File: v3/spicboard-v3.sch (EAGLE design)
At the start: 39 parts, among them IC1 74HC595N, Q1 BC557, Q2 BC557

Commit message: OLED1 ausgetauscht
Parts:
- OLED1: device pinhead:PINHD-1X4 -> SparkFun-Connectors:CONN_04
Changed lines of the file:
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@@
 <part name="GND7" library="supply1" deviceset="GND" device=""/>
 <part name="EXT" library="pinhead" deviceset="PINHD-1X4" device=""/>
-<part name="OLED1" library="pinhead" deviceset="PINHD-1X4" device=""/>
 <part name="OLED2" library="pinhead" deviceset="PINHD-1X4" device=""/>
 <part name="COM" library="pinhead" deviceset="PINHD-1X3" device=""/>
@@
 <part name="BTN0" library="switch-omron" deviceset="10-XX" device=""/>
 <part name="BTN1" library="switch-omron" deviceset="10-XX" device=""/>
+<part name="OLED1" library="SparkFun-Connectors" deviceset="CONN_04" device=""/>
 </parts>
 <sheets>
@@
 <instance part="GND7" gate="1" x="137.16" y="-10.16"/>
 <instance part="EXT" gate="A" x="48.26" y="-20.32"/>
-<instance part="OLED1" gate="A" x="48.26" y="-2.54"/>
 <instance part="OLED2" gate="A" x="81.28" y="-2.54"/>
 <instance part="COM" gate="A" x="81.28" y="-17.78"/>
@@
 <instance part="BTN0" gate="1" x="129.54" y="0"/>
 <instance part="BTN1" gate="1" x="172.72" y="0"/>
+<instance part="OLED1" gate="G$1" x="43.18" y="0" rot="R180"/>
 </instances>
 <busses>
@@
 </segment>
 <segment>
-<pinref part="OLED1" gate="A" pin="2"/>
-<wire x1="27.94" y1="0" x2="45.72" y2="0" width="0.1524" layer="91"/>
+<wire x1="27.94" y1="0" x2="38.1" y2="0" width="0.1524" layer="91"/>
 <label x="27.94" y="0" size="1.778" layer="95"/>
+<pinref part="OLED1" gate="G$1" pin="2"/>
 </segment>
 <segment>
@@
 </segment>
 <segment>
-<pinref part="OLED1" gate="A" pin="1"/>
-<wire x1="45.72" y1="2.54" x2="27.94" y2="2.54" width="0.1524" layer="91"/>
 <label x="27.94" y="2.54" size="1.778" layer="95"/>
+<pinref part="OLED1" gate="G$1" pin="1"/>
+<wire x1="38.1" y1="2.54" x2="27.94" y2="2.54" width="0.1524" layer="91"/>
 </segment>
 <segment>
@@
 </segment>
 <segment>
-<pinref part="OLED1" gate="A" pin="4"/>
-<wire x1="27.94" y1="-5.08" x2="45.72" y2="-5.08" width="0.1524" layer="91"/>
+<wire x1="27.94" y1="-5.08" x2="38.1" y2="-5.08" width="0.1524" layer="91"/>
 <label x="27.94" y="-5.08" size="1.778" layer="95"/>
+<pinref part="OLED1" gate="G$1" pin="4"/>
 </segment>
 <segment>
@@
 </segment>
 <segment>
-<pinref part="OLED1" gate="A" pin="3"/>
-<wire x1="45.72" y1="-2.54" x2="27.94" y2="-2.54" width="0.1524" layer="91"/>
 <label x="27.94" y="-2.54" size="1.778" layer="95"/>
-</segment>
-<segment>
+<pinref part="OLED1" gate="G$1" pin="3"/>
+<wire x1="38.1" y1="-2.54" x2="27.94" y2="-2.54" width="0.1524" layer="91"/>
+</segment>
+<segment>

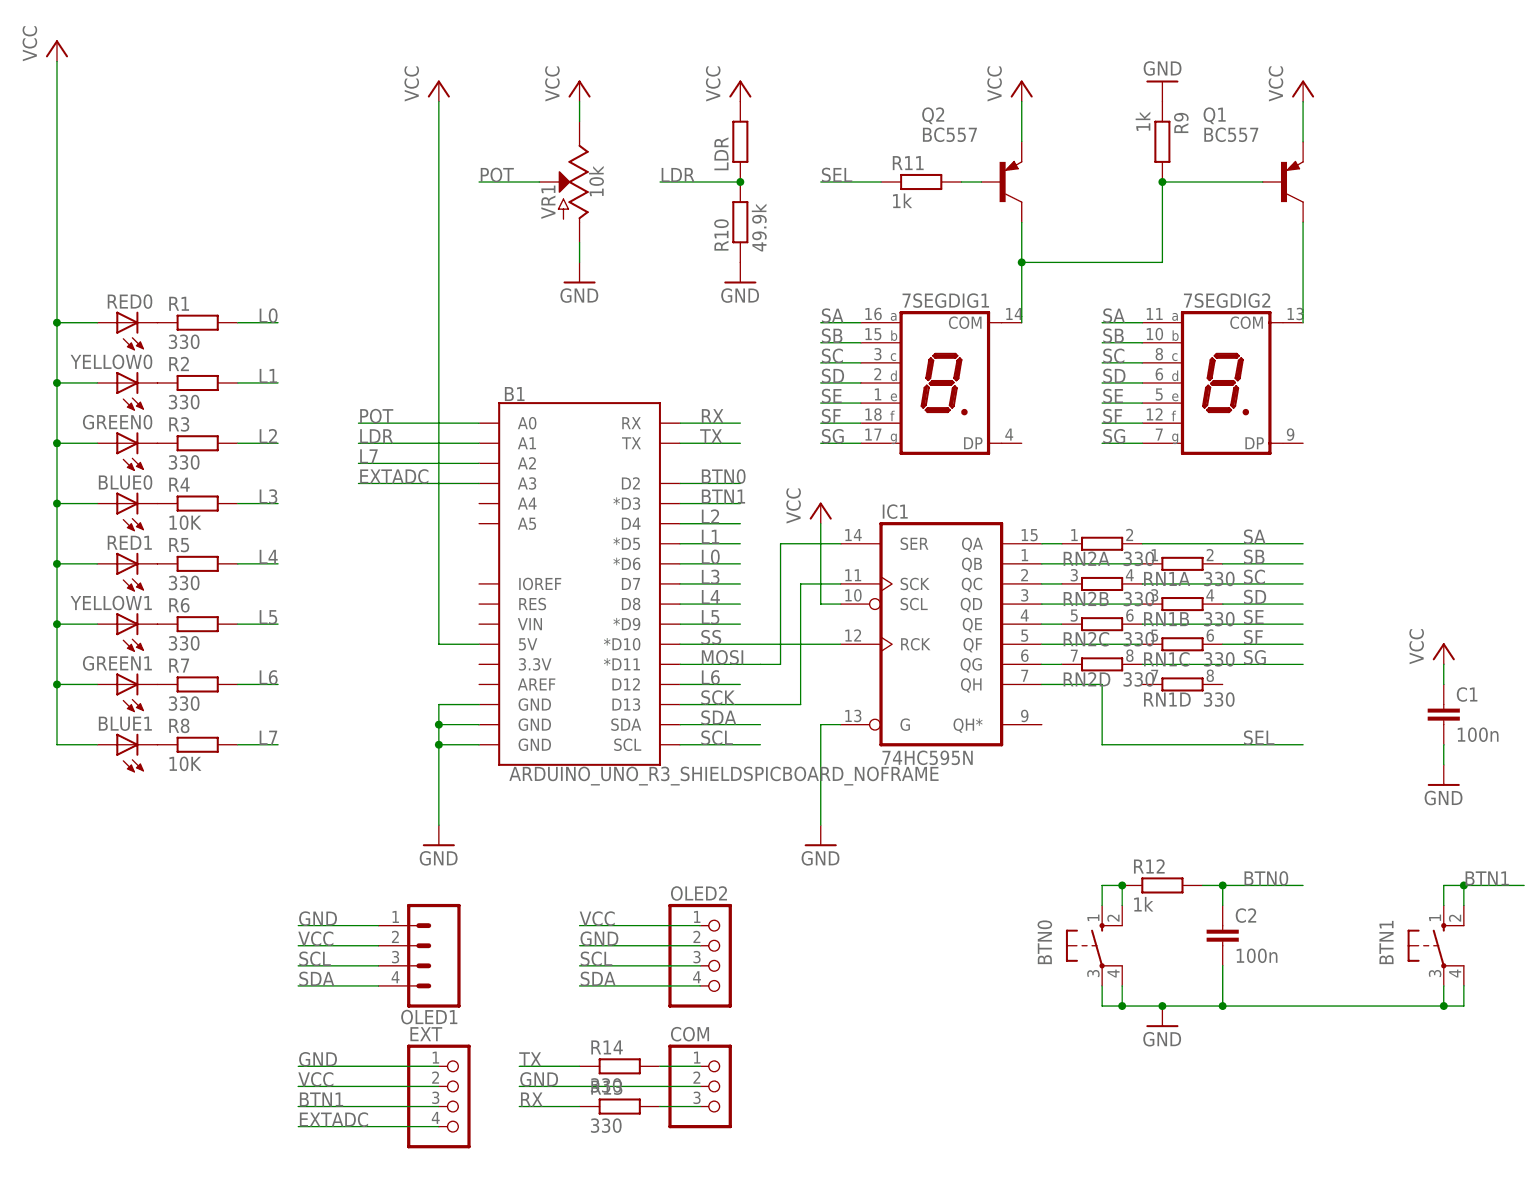
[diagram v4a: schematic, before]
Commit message: OLED/EXT/COM ausgetauscht
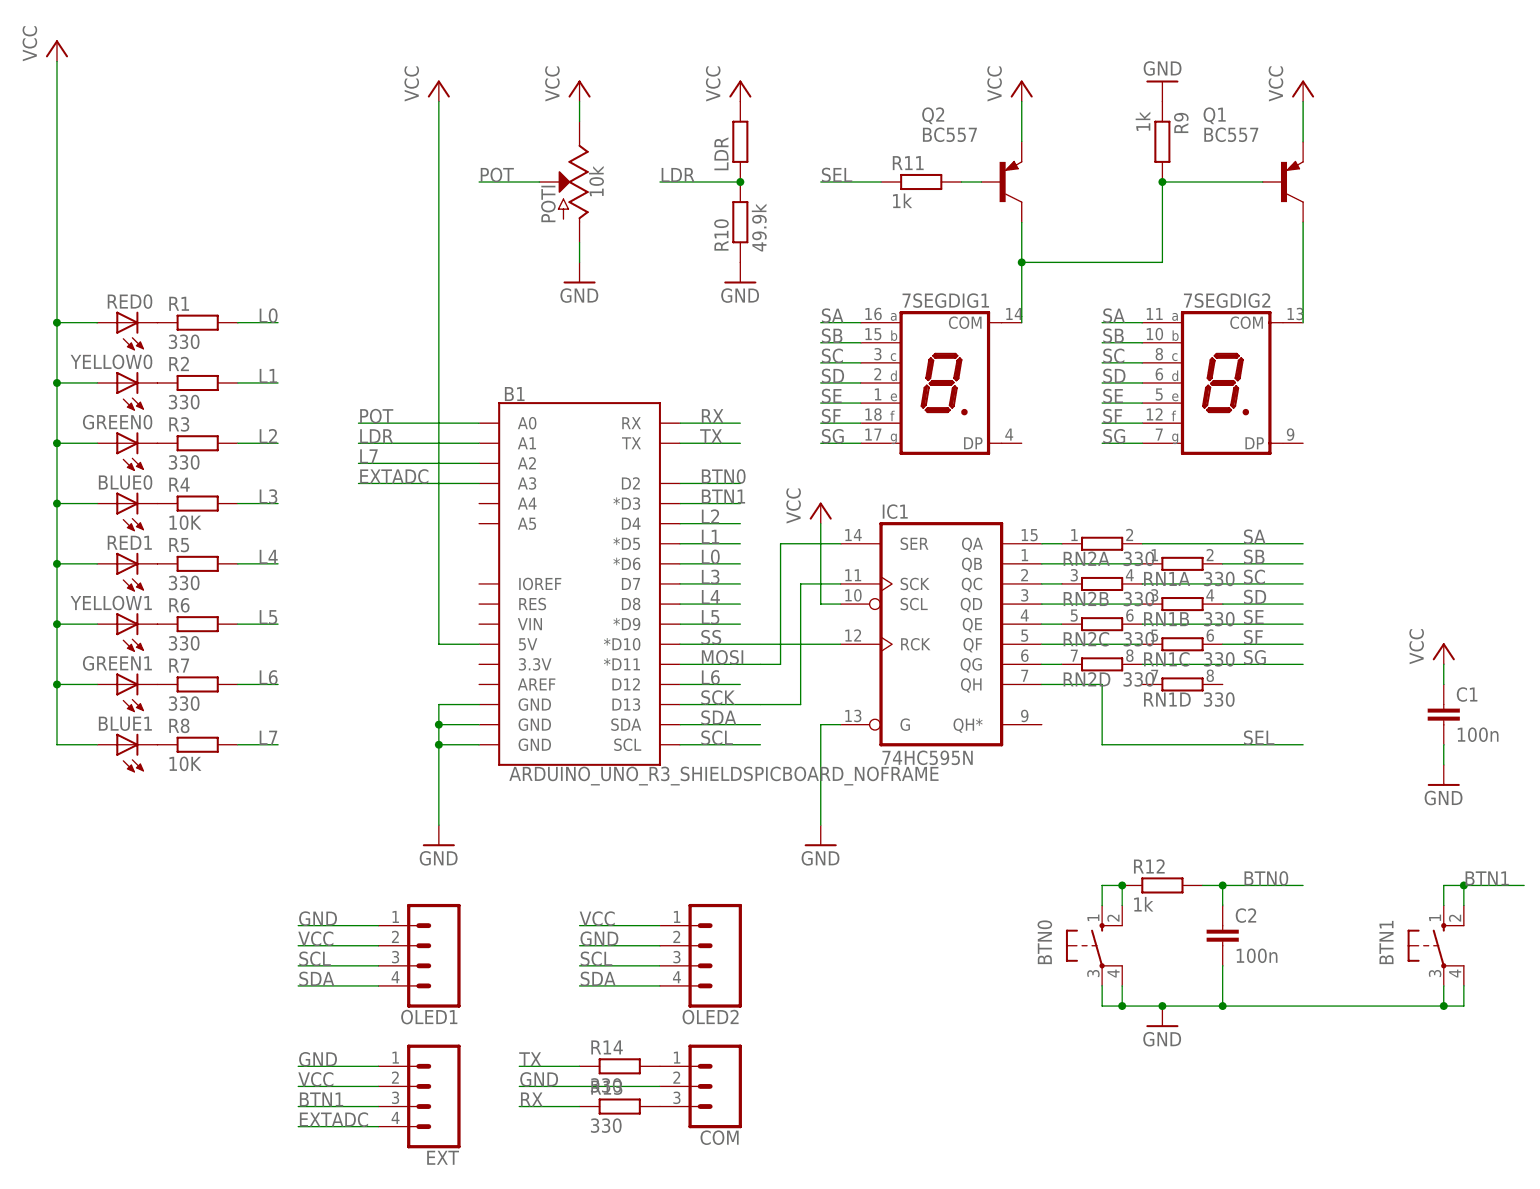
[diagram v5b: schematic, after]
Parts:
- COM: device pinhead:PINHD-1X3 -> SparkFun-Connectors:CONN_03
- EXT, OLED2: device pinhead:PINHD-1X4 -> SparkFun-Connectors:CONN_04
- renumbered VR1 to POTI
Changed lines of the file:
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@@
 <part name="IC1" library="74xx-eu" deviceset="74*595" device="N" technology="HC"/>
 <part name="LDR" library="spicboard-v3" deviceset="LDR" device="LDR" value=""/>
-<part name="VR1" library="spicboard-v3" deviceset="POTENTIOMETER" device="-PTH-9MM-1/20W-20%" value="10k"/>
+<part name="POTI" library="spicboard-v3" deviceset="POTENTIOMETER" device="-PTH-9MM-1/20W-20%" value="10k"/>
 <part name="RN1" library="resistor-sil" deviceset="E4R" device="" value="330"/>
 <part name="RN2" library="resistor-sil" deviceset="E4R" device="" value="330"/>
@@
 <part name="C2" library="capacitor-wima" deviceset="C" device="2.5/2" value="100n"/>
 <part name="GND7" library="supply1" deviceset="GND" device=""/>
-<part name="EXT" library="pinhead" deviceset="PINHD-1X4" device=""/>
-<part name="OLED2" library="pinhead" deviceset="PINHD-1X4" device=""/>
-<part name="COM" library="pinhead" deviceset="PINHD-1X3" device=""/>
 <part name="R13" library="resistor" deviceset="R-EU_" device="0207/10" value="330"/>
 <part name="R14" library="resistor" deviceset="R-EU_" device="0207/10" value="330"/>
@@
 <part name="BTN1" library="switch-omron" deviceset="10-XX" device=""/>
 <part name="OLED1" library="SparkFun-Connectors" deviceset="CONN_04" device=""/>
+<part name="OLED2" library="SparkFun-Connectors" deviceset="CONN_04" device=""/>
+<part name="EXT" library="SparkFun-Connectors" deviceset="CONN_04" device=""/>
+<part name="COM" library="SparkFun-Connectors" deviceset="CONN_03" device=""/>
 </parts>
 <sheets>
@@
 <instance part="IC1" gate="A" x="109.22" y="40.64"/>
 <instance part="LDR" gate="G$1" x="83.82" y="101.6" rot="R90"/>
-<instance part="VR1" gate="G$1" x="63.5" y="96.52" rot="MR0"/>
+<instance part="POTI" gate="G$1" x="63.5" y="96.52" rot="MR0"/>
 <instance part="RN1" gate="A" x="139.7" y="48.26"/>
 <instance part="RN1" gate="B" x="139.7" y="43.18"/>
@@
 <instance part="C2" gate="G$1" x="144.78" y="2.54"/>
 <instance part="GND7" gate="1" x="137.16" y="-10.16"/>
-<instance part="EXT" gate="A" x="48.26" y="-20.32"/>
-<instance part="OLED2" gate="A" x="81.28" y="-2.54"/>
-<instance part="COM" gate="A" x="81.28" y="-17.78"/>
 <instance part="R13" gate="G$1" x="68.58" y="-20.32"/>
 <instance part="R14" gate="G$1" x="68.58" y="-15.24"/>
@@
 <instance part="BTN1" gate="1" x="172.72" y="0"/>
 <instance part="OLED1" gate="G$1" x="43.18" y="0" rot="R180"/>
+<instance part="OLED2" gate="G$1" x="78.74" y="0" rot="R180"/>
+<instance part="EXT" gate="G$1" x="43.18" y="-17.78" rot="R180"/>
+<instance part="COM" gate="J$1" x="81.28" y="-17.78" rot="R180"/>
 </instances>
 <busses>
@@
 </segment>
 <segment>
-<pinref part="VR1" gate="G$1" pin="E"/>
+<pinref part="POTI" gate="G$1" pin="E"/>
 <pinref part="P+4" gate="VCC" pin="VCC"/>
 <wire x1="63.5" y1="104.14" x2="63.5" y2="106.68" width="0.1524" layer="91"/>
@@
 </segment>
 <segment>
-<pinref part="OLED2" gate="A" pin="1"/>
-<wire x1="78.74" y1="2.54" x2="63.5" y2="2.54" width="0.1524" layer="91"/>
+<wire x1="73.66" y1="2.54" x2="63.5" y2="2.54" width="0.1524" layer="91"/>
 <label x="63.5" y="2.54" size="1.778" layer="95"/>
-</segment>
-<segment>
-<pinref part="EXT" gate="A" pin="2"/>
-<wire x1="45.72" y1="-17.78" x2="27.94" y2="-17.78" width="0.1524" layer="91"/>
+<pinref part="OLED2" gate="G$1" pin="1"/>
+</segment>
+<segment>
+<wire x1="38.1" y1="-17.78" x2="27.94" y2="-17.78" width="0.1524" layer="91"/>
 <label x="27.94" y="-17.78" size="1.778" layer="95"/>
+<pinref part="EXT" gate="G$1" pin="2"/>
 </segment>
 <segment>
@@
 </segment>
 <segment>
-<pinref part="VR1" gate="G$1" pin="A"/>
+<pinref part="POTI" gate="G$1" pin="A"/>
 <pinref part="GND2" gate="1" pin="GND"/>
 <wire x1="63.5" y1="88.9" x2="63.5" y2="86.36" width="0.1524" layer="91"/>
@@
 </segment>
 <segment>
-<pinref part="OLED2" gate="A" pin="2"/>
-<wire x1="78.74" y1="0" x2="63.5" y2="0" width="0.1524" layer="91"/>
+<wire x1="73.66" y1="0" x2="63.5" y2="0" width="0.1524" layer="91"/>
 <label x="63.5" y="0" size="1.778" layer="95"/>
-</segment>
-<segment>
-<pinref part="COM" gate="A" pin="2"/>
-<wire x1="78.74" y1="-17.78" x2="55.88" y2="-17.78" width="0.1524" layer="91"/>
+<pinref part="OLED2" gate="G$1" pin="2"/>
+</segment>
+<segment>
+<wire x1="73.66" y1="-17.78" x2="55.88" y2="-17.78" width="0.1524" layer="91"/>
 <label x="55.88" y="-17.78" size="1.778" layer="95"/>
-</segment>
-<segment>
-<pinref part="EXT" gate="A" pin="1"/>
-<wire x1="45.72" y1="-15.24" x2="27.94" y2="-15.24" width="0.1524" layer="91"/>
+<pinref part="COM" gate="J$1" pin="2"/>
+</segment>
+<segment>
+<wire x1="38.1" y1="-15.24" x2="27.94" y2="-15.24" width="0.1524" layer="91"/>
 <label x="27.94" y="-15.24" size="1.778" layer="95"/>
+<pinref part="EXT" gate="G$1" pin="1"/>
 </segment>
 </net>
@@
 <net name="POT" class="0">
 <segment>
-<pinref part="VR1" gate="G$1" pin="S"/>
+<pinref part="POTI" gate="G$1" pin="S"/>
 <wire x1="58.42" y1="96.52" x2="50.8" y2="96.52" width="0.1524" layer="91"/>
 <label x="50.8" y="96.52" size="1.778" layer="95"/>
@@
 </segment>
 <segment>
-<pinref part="EXT" gate="A" pin="3"/>
-<wire x1="45.72" y1="-20.32" x2="27.94" y2="-20.32" width="0.1524" layer="91"/>
+<wire x1="38.1" y1="-20.32" x2="27.94" y2="-20.32" width="0.1524" layer="91"/>
 <label x="27.94" y="-20.32" size="1.778" layer="95"/>
+<pinref part="EXT" gate="G$1" pin="3"/>
 </segment>
 </net>
 <net name="EXTADC" class="0">
 <segment>
-<pinref part="EXT" gate="A" pin="4"/>
-<wire x1="45.72" y1="-22.86" x2="27.94" y2="-22.86" width="0.1524" layer="91"/>
+<wire x1="38.1" y1="-22.86" x2="27.94" y2="-22.86" width="0.1524" layer="91"/>
 <label x="27.94" y="-22.86" size="1.778" layer="95"/>
+<pinref part="EXT" gate="G$1" pin="4"/>
 </segment>
 <segment>
@@
 </segment>
 <segment>
-<pinref part="OLED2" gate="A" pin="4"/>
-<wire x1="78.74" y1="-5.08" x2="63.5" y2="-5.08" width="0.1524" layer="91"/>
+<wire x1="73.66" y1="-5.08" x2="63.5" y2="-5.08" width="0.1524" layer="91"/>
 <label x="63.5" y="-5.08" size="1.778" layer="95"/>
+<pinref part="OLED2" gate="G$1" pin="4"/>
 </segment>
 </net>
@@
 </segment>
 <segment>
-<pinref part="OLED2" gate="A" pin="3"/>
-<wire x1="78.74" y1="-2.54" x2="63.5" y2="-2.54" width="0.1524" layer="91"/>
+<wire x1="73.66" y1="-2.54" x2="63.5" y2="-2.54" width="0.1524" layer="91"/>
 <label x="63.5" y="-2.54" size="1.778" layer="95"/>
+<pinref part="OLED2" gate="G$1" pin="3"/>
 </segment>
 </net>
@@
 <net name="N$15" class="0">
 <segment>
-<pinref part="COM" gate="A" pin="1"/>
-<wire x1="78.74" y1="-15.24" x2="73.66" y2="-15.24" width="0.1524" layer="91"/>
 <pinref part="R14" gate="G$1" pin="2"/>
+<pinref part="COM" gate="J$1" pin="1"/>
 </segment>
 </net>
 <net name="N$21" class="0">
 <segment>
-<pinref part="COM" gate="A" pin="3"/>
-<wire x1="78.74" y1="-20.32" x2="73.66" y2="-20.32" width="0.1524" layer="91"/>
 <pinref part="R13" gate="G$1" pin="2"/>
-</segment>
-</net>
+<pinref part="COM" gate="J$1" pin="3"/>
+</segment>
+</net>

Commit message: SPiCboard: i4logo, LDR -> PHOTO, TODOs aktualisiert
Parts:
- renumbered LDR to PHOTO
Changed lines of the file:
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@@
 <part name="R8" library="resistor" deviceset="R-EU_" device="0207/10" value="10K"/>
 <part name="IC1" library="74xx-eu" deviceset="74*595" device="N" technology="HC"/>
-<part name="LDR" library="spicboard-v3" deviceset="LDR" device="LDR" value=""/>
+<part name="PHOTO" library="spicboard-v3" deviceset="LDR" device="LDR" value=""/>
 <part name="POTI" library="spicboard-v3" deviceset="POTENTIOMETER" device="-PTH-9MM-1/20W-20%" value="10k"/>
 <part name="RN1" library="resistor-sil" deviceset="E4R" device="" value="330"/>
@@
 <instance part="R8" gate="G$1" x="15.24" y="25.4"/>
 <instance part="IC1" gate="A" x="109.22" y="40.64"/>
-<instance part="LDR" gate="G$1" x="83.82" y="101.6" rot="R90"/>
+<instance part="PHOTO" gate="G$1" x="83.82" y="101.6" rot="R90"/>
 <instance part="POTI" gate="G$1" x="63.5" y="96.52" rot="MR0"/>
 <instance part="RN1" gate="A" x="139.7" y="48.26"/>
@@
 <segment>
 <pinref part="P+5" gate="VCC" pin="VCC"/>
-<pinref part="LDR" gate="G$1" pin="2"/>
+<pinref part="PHOTO" gate="G$1" pin="2"/>
 </segment>
 <segment>
@@
 <segment>
 <pinref part="R10" gate="G$1" pin="2"/>
-<pinref part="LDR" gate="G$1" pin="1"/>
+<pinref part="PHOTO" gate="G$1" pin="1"/>
 <wire x1="83.82" y1="96.52" x2="73.66" y2="96.52" width="0.1524" layer="91"/>
 <label x="73.66" y="96.52" size="1.778" layer="95"/>

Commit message: SPiCboard: Markierung am Widerstandsnetzwerk entfernt
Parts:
- RN1, RN2: device resistor-sil:E4R -> spicboard-v3:E4R
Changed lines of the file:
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@@
 <part name="PHOTO" library="spicboard-v3" deviceset="LDR" device="LDR" value=""/>
 <part name="POTI" library="spicboard-v3" deviceset="POTENTIOMETER" device="-PTH-9MM-1/20W-20%" value="10k"/>
-<part name="RN1" library="resistor-sil" deviceset="E4R" device="" value="330"/>
-<part name="RN2" library="resistor-sil" deviceset="E4R" device="" value="330"/>
+<part name="RN1" library="spicboard-v3" deviceset="E4R" device="" value="330"/>
+<part name="RN2" library="spicboard-v3" deviceset="E4R" device="" value="330"/>
 <part name="Q1" library="transistor-pnp" deviceset="BC557*" device=""/>
 <part name="Q2" library="transistor-pnp" deviceset="BC557*" device=""/>

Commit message: SPiCboard: Beschriftung verschoben
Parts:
- B1: value ARDUINO_UNO_R3_SHIELDSPICBOARD_NOFRAME -> ARDUINO_UNO_R3_SHIELD; device spicboard-v3:ARDUINO_UNO_R3_SHIELDSPICBOARD_NOFRAME -> spicboard-v3:ARDUINO_UNO_R3_SHIELD
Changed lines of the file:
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@@
 </classes>
 <parts>
-<part name="B1" library="spicboard-v3" deviceset="ARDUINO_UNO_R3_SHIELD" device="SPICBOARD_NOFRAME" value="ARDUINO_UNO_R3_SHIELDSPICBOARD_NOFRAME"/>
+<part name="B1" library="spicboard-v3" deviceset="ARDUINO_UNO_R3_SHIELD" device="" value="ARDUINO_UNO_R3_SHIELD"/>
 <part name="RED0" library="led" deviceset="LED" device="5MM"/>
 <part name="YELLOW0" library="led" deviceset="LED" device="5MM"/>
